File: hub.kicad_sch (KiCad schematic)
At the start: 0 parts

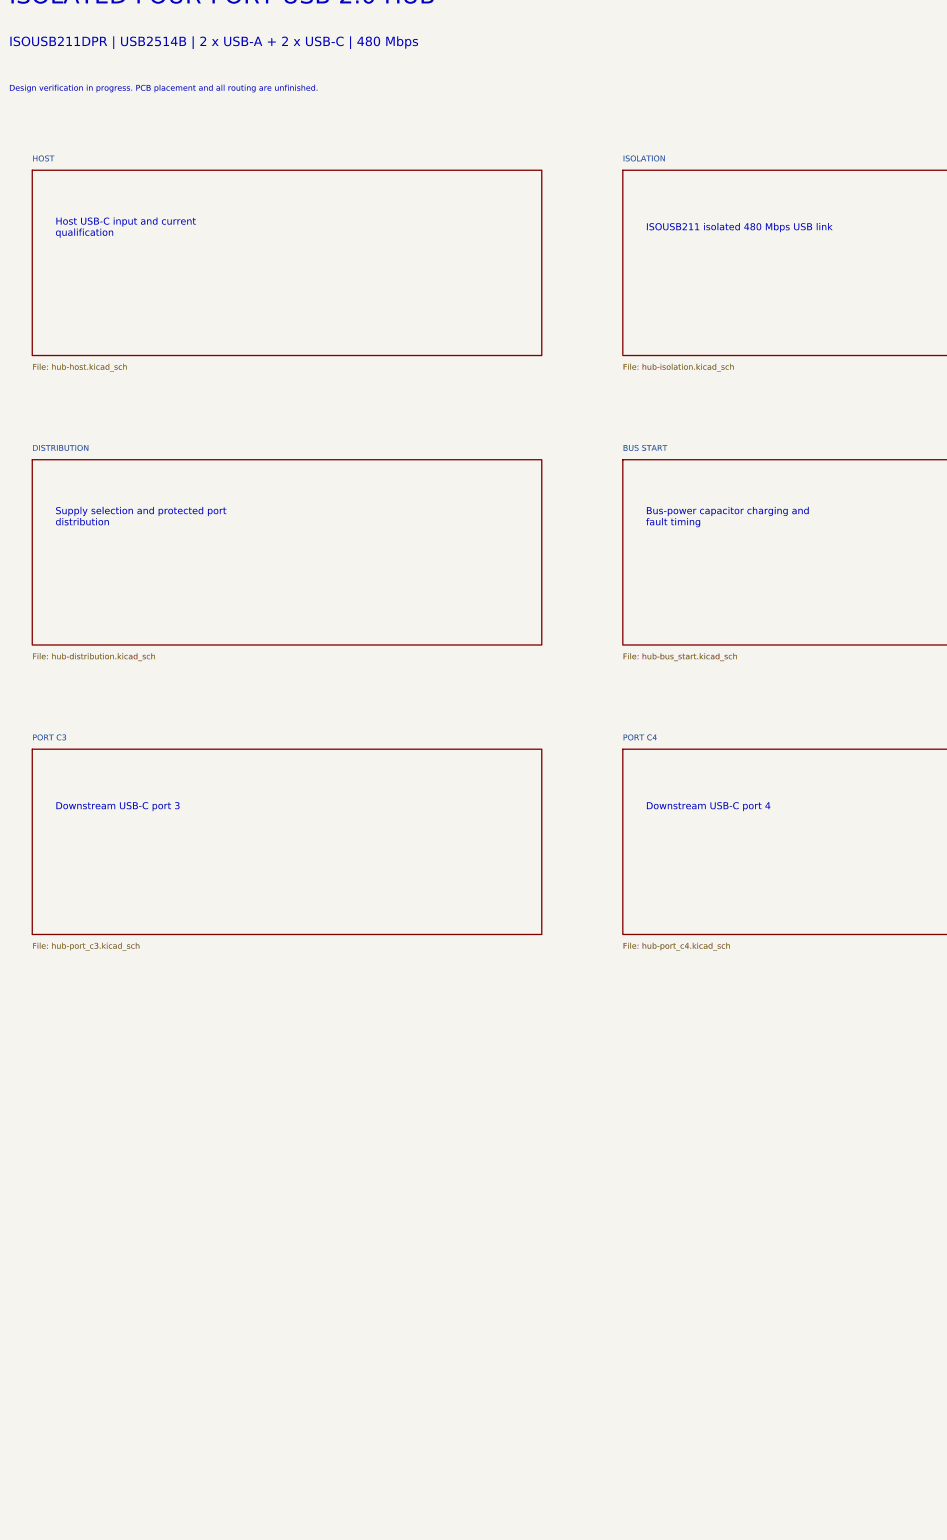
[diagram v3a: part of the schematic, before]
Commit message: feat(revc): finish verified TI hub routing handoff
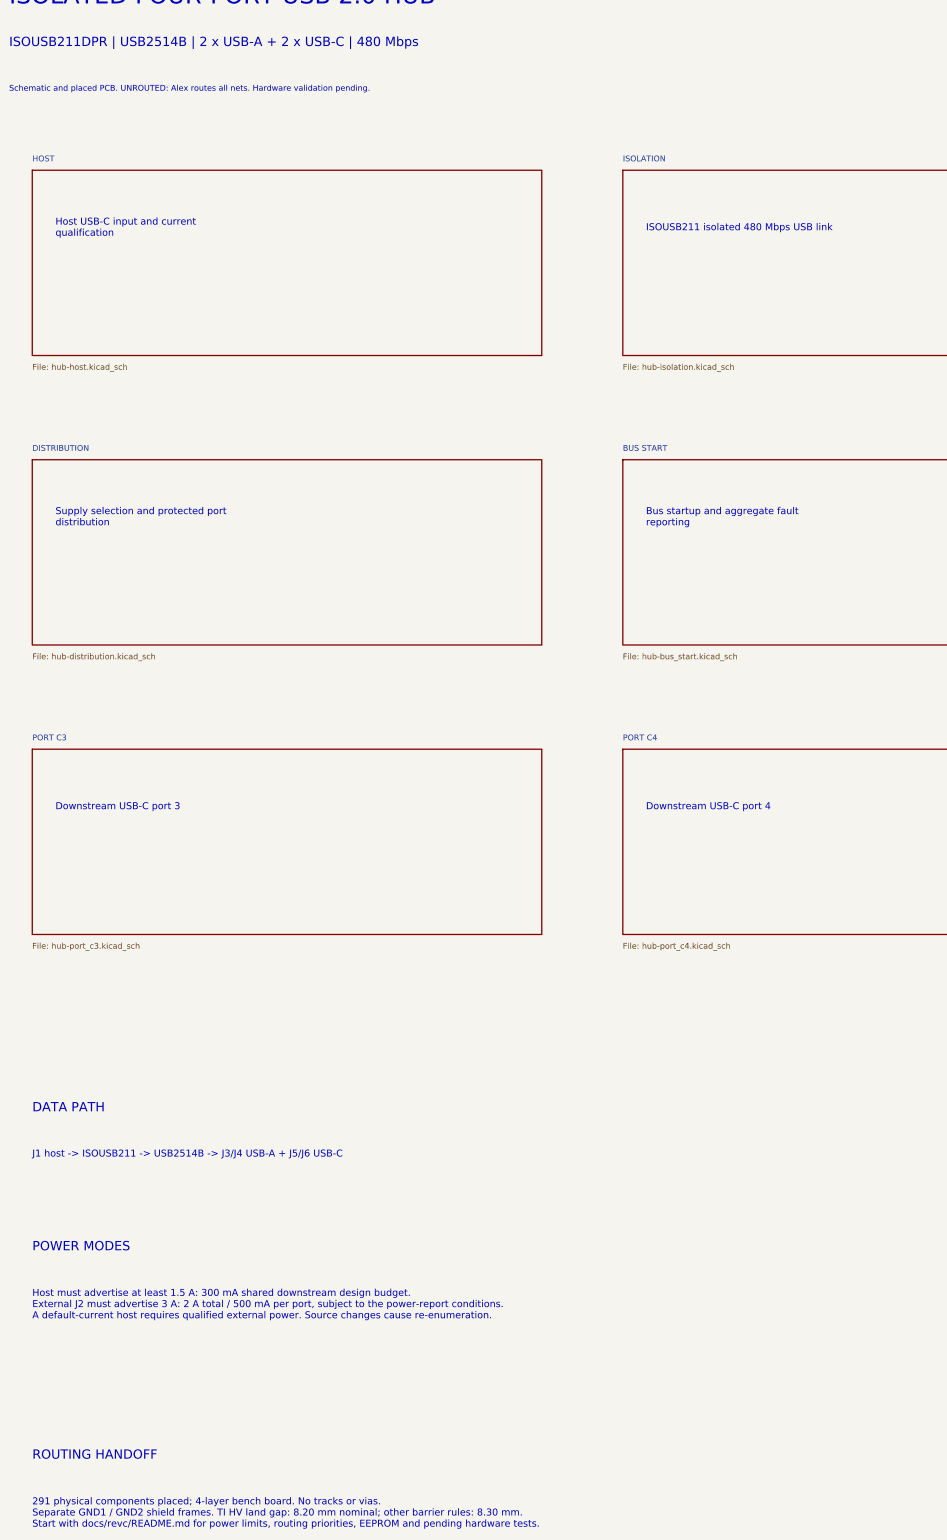
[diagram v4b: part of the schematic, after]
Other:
- note added: "291 physical components placed; 4-layer bench board. No tracks or vias. Separate GND1 / GND2 shield frames. TI HV land gap: 8.20 mm nominal; other barrier rules: 8.30 mm. Start with docs/revc/README.md for power limits, routing priorities, EEPROM and pending hardware tests."
- note added: "Bus startup and aggregate fault reporting"
- note added: "DATA PATH"
- note added: "Host must advertise at least 1.5 A: 300 mA shared downstream design budget. External J2 must advertise 3 A: 2 A total / 500 mA per port, subject to the power-report conditions. A default-current host requires qualified external power. Source changes cause re-enumeration."
- note added: "J1 host -> ISOUSB211 -> USB2514B -> J3/J4 USB-A + J5/J6 USB-C"
- note added: "POWER MODES"
- note added: "ROUTING HANDOFF"
- note added: "Schematic and placed PCB. UNROUTED: Alex routes all nets. Hardware validation pending."
- note removed: "Bus-power capacitor charging and fault timing"
- note removed: "Design verification in progress. PCB placement and all routing are unfinished."
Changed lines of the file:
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@@
   (title_block
     (title "Rev C — Isolated four-port USB 2.0 hub")
-    (rev "C — verification in progress")
+    (rev "C")
     (date "2026-09-10")
   )
@@
     )
   )
-  (text "Design verification in progress. PCB placement and all routing are unfinished."
+  (text "Schematic and placed PCB. UNROUTED: Alex routes all nets. Hardware validation pending."
     (at 15.24 38.1 0)
     (effects
@@
     )
   )
-  (text "Bus-power capacitor charging and\nfault timing"
+  (text "Bus startup and aggregate fault\nreporting"
     (at 154.94 132.07999999999998 0)
     (effects
@@
     (effects
       (font
+        (size 1.524 1.524)
+      )
+      (justify left)
+    )
+  )
+  (text "DATA PATH"
+    (at 20.32 261.62 0)
+    (effects
+      (font
+        (size 2.032 2.032)
+      )
+      (justify left)
+    )
+  )
+  (text "J1 host -> ISOUSB211 -> USB2514B -> J3/J4 USB-A + J5/J6 USB-C"
+    (at 20.32 271.78 0)
+    (effects
+      (font
+        (size 1.524 1.524)
+      )
+      (justify left)
+    )
+  )
+  (text "POWER MODES"
+    (at 20.32 292.1 0)
+    (effects
+      (font
+        (size 2.032 2.032)
+      )
+      (justify left)
+    )
+  )
+  (text "Host must advertise at least 1.5 A: 300 mA shared downstream design budget.\nExternal J2 must advertise 3 A: 2 A total / 500 mA per port, subject to the power-report conditions.\nA default-current host requires qualified external power. Source changes cause re-enumeration."
+    (at 20.32 304.8 0)
+    (effects
+      (font
+        (size 1.524 1.524)
+      )
+      (justify left)
+    )
+  )
+  (text "ROUTING HANDOFF"
+    (at 20.32 337.82 0)
+    (effects
+      (font
+        (size 2.032 2.032)
+      )
+      (justify left)
+    )
+  )
+  (text "291 physical components placed; 4-layer bench board. No tracks or vias.\nSeparate GND1 / GND2 shield frames. TI HV land gap: 8.20 mm nominal; other barrier rules: 8.30 mm.\nStart with docs/revc/README.md for power limits, routing priorities, EEPROM and pending hardware tests."
+    (at 20.32 350.52 0)
+    (effects
+      (font
